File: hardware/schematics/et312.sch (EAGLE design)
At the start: 12 parts, among them IC1 MEGA16-P, IC2 4066N, X1 HD44780LCD-1602

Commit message: Updated Schematics
WIP
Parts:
- added JTAG: (no value), pinhead:PINHD-2X8
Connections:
- removed net N$9: 10WAY_RIBBON1.6
- new net 5V: 10WAY_RIBBON1.6, IC1.AREF, IC1.AVCC, IC1.VCC, IC2P.VDD, S1.P, S3.P
- new net JTAG11: JTAG.11
- new net JTAG13: JTAG.13
- new net JTAG15-RESET: IC1.RESET, JTAG.15
- new net JTAG7: JTAG.7
- new net JTAG9: JTAG.9
- new net N$6: IC1.(MISO)PB6
- new net PA1: 10WAY_RIBBON1.3, IC1.(ADC1)PA1
- new net PA4: 10WAY_RIBBON1.8, IC1.(ADC4)PA4
- new net PA5: 10WAY_RIBBON1.7, IC1.(ADC5)PA5
- net GND: now also 10WAY_RIBBON1.5, IC1.GND@1, IC2P.VSS

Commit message: PCB WIP
Added more to the PCB
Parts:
- added LED1, LED2: (no value), adafruit:LED3MM
- renumbered IC1 to U1, JTAG to J2
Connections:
- new net N$9: U1.(SS)PB4
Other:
- note added: "16 Way IDC connector"
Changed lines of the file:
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@@
 <?xml version="1.0" encoding="utf-8"?>
 <!DOCTYPE eagle SYSTEM "eagle.dtd">
-<eagle version="7.1.0">
+<eagle version="7.3.0">
 <drawing>
 <settings>
@@
 <part name="VR3" library="SparkFun-Electromechanical" deviceset="POT" device=""/>
 <part name="RV2" library="SparkFun-Electromechanical" deviceset="POT" device=""/>
-<part name="IC1" library="atmel" deviceset="MEGA16-P" device=""/>
+<part name="U1" library="atmel" deviceset="MEGA16-P" device=""/>
 <part name="S1" library="adafruit" deviceset="SPST" device=""/>
 <part name="S3" library="adafruit" deviceset="SPST" device=""/>
@@
 <part name="SUPPLY4" library="SparkFun-Aesthetics" deviceset="5V" device=""/>
 <part name="SUPPLY5" library="SparkFun-Aesthetics" deviceset="5V" device=""/>
-<part name="JTAG" library="pinhead" deviceset="PINHD-2X8" device=""/>
+<part name="J2" library="pinhead" deviceset="PINHD-2X8" device=""/>
+<part name="LED1" library="adafruit" deviceset="LED" device="3MM"/>
+<part name="LED2" library="adafruit" deviceset="LED" device="3MM"/>
+<part name="GND4" library="SparkFun-Aesthetics" deviceset="GND" device=""/>
 </parts>
 <sheets>
@@
 <sheet>
 <plain>
+<text x="35.56" y="119.38" size="1.778" layer="91">16 Way IDC connector</text>
 </plain>
 <instances>
 <instance part="FRAME1" gate="G$1" x="0" y="0"/>
 <instance part="GND1" gate="1" x="101.6" y="43.18"/>
-<instance part="IC1" gate="G$1" x="127" y="104.14"/>
+<instance part="U1" gate="G$1" x="127" y="104.14"/>
 <instance part="SUPPLY5" gate="G$1" x="99.06" y="149.86"/>
-<instance part="JTAG" gate="A" x="50.8" y="137.16"/>
+<instance part="J2" gate="A" x="50.8" y="137.16"/>
+<instance part="LED1" gate="G$1" x="205.74" y="71.12"/>
+<instance part="LED2" gate="G$1" x="215.9" y="71.12"/>
+<instance part="GND4" gate="1" x="210.82" y="43.18"/>
 </instances>
 <busses>
@@
 <net name="GND" class="0">
 <segment>
-<pinref part="IC1" gate="G$1" pin="GND"/>
+<pinref part="U1" gate="G$1" pin="GND"/>
 <wire x1="106.68" y1="114.3" x2="101.6" y2="114.3" width="0.1524" layer="91"/>
 <wire x1="101.6" y1="114.3" x2="101.6" y2="45.72" width="0.1524" layer="91"/>
 <pinref part="GND1" gate="1" pin="GND"/>
-<pinref part="IC1" gate="G$1" pin="GND@1"/>
+<pinref part="U1" gate="G$1" pin="GND@1"/>
 <wire x1="106.68" y1="121.92" x2="101.6" y2="121.92" width="0.1524" layer="91"/>
 <wire x1="101.6" y1="121.92" x2="101.6" y2="114.3" width="0.1524" layer="91"/>
@@
 <net name="PC0" class="0">
 <segment>
-<pinref part="IC1" gate="G$1" pin="(SCL)PC0"/>
+<pinref part="U1" gate="G$1" pin="(SCL)PC0"/>
 <wire x1="147.32" y1="81.28" x2="157.48" y2="81.28" width="0.1524" layer="91"/>
 <label x="157.48" y="81.28" size="1.778" layer="95" xref="yes"/>
@@
 <net name="PC4" class="0">
 <segment>
-<pinref part="IC1" gate="G$1" pin="(TDO)PC4"/>
+<pinref part="U1" gate="G$1" pin="(TDO)PC4"/>
 <wire x1="147.32" y1="91.44" x2="157.48" y2="91.44" width="0.1524" layer="91"/>
 <label x="157.48" y="91.44" size="1.778" layer="95" xref="yes"/>
@@
 <net name="PC5" class="0">
 <segment>
-<pinref part="IC1" gate="G$1" pin="(TDI)PC5"/>
+<pinref part="U1" gate="G$1" pin="(TDI)PC5"/>
 <wire x1="147.32" y1="93.98" x2="157.48" y2="93.98" width="0.1524" layer="91"/>
 <label x="157.48" y="93.98" size="1.778" layer="95" xref="yes"/>
@@
 <net name="PC6" class="0">
 <segment>
-<pinref part="IC1" gate="G$1" pin="(TOSC1)PC6"/>
+<pinref part="U1" gate="G$1" pin="(TOSC1)PC6"/>
 <wire x1="147.32" y1="96.52" x2="157.48" y2="96.52" width="0.1524" layer="91"/>
 <label x="157.48" y="96.52" size="1.778" layer="95" xref="yes"/>
@@
 <net name="PC7" class="0">
 <segment>
-<pinref part="IC1" gate="G$1" pin="(TOSC2)PC7"/>
+<pinref part="U1" gate="G$1" pin="(TOSC2)PC7"/>
 <wire x1="147.32" y1="99.06" x2="157.48" y2="99.06" width="0.1524" layer="91"/>
 <label x="157.48" y="99.06" size="1.778" layer="95" xref="yes"/>
@@
 <net name="PC3" class="0">
 <segment>
-<pinref part="IC1" gate="G$1" pin="(TMS)PC3"/>
+<pinref part="U1" gate="G$1" pin="(TMS)PC3"/>
 <wire x1="147.32" y1="88.9" x2="157.48" y2="88.9" width="0.1524" layer="91"/>
 <label x="157.48" y="88.9" size="1.778" layer="95" xref="yes"/>
@@
 <net name="PC2" class="0">
 <segment>
-<pinref part="IC1" gate="G$1" pin="(TCK)PC2"/>
+<pinref part="U1" gate="G$1" pin="(TCK)PC2"/>
 <wire x1="147.32" y1="86.36" x2="157.48" y2="86.36" width="0.1524" layer="91"/>
 <label x="157.48" y="86.36" size="1.778" layer="95" xref="yes"/>
@@
 <net name="PC1" class="0">
 <segment>
-<pinref part="IC1" gate="G$1" pin="(SDA)PC1"/>
+<pinref part="U1" gate="G$1" pin="(SDA)PC1"/>
 <wire x1="147.32" y1="83.82" x2="157.48" y2="83.82" width="0.1524" layer="91"/>
 <label x="157.48" y="83.82" size="1.778" layer="95" xref="yes"/>
@@
 <net name="PA5" class="0">
 <segment>
-<pinref part="IC1" gate="G$1" pin="(ADC5)PA5"/>
+<pinref part="U1" gate="G$1" pin="(ADC5)PA5"/>
 <wire x1="147.32" y1="139.7" x2="157.48" y2="139.7" width="0.1524" layer="91"/>
 <label x="157.48" y="139.7" size="1.778" layer="95" xref="yes"/>
@@
 <net name="PA4" class="0">
 <segment>
-<pinref part="IC1" gate="G$1" pin="(ADC4)PA4"/>
+<pinref part="U1" gate="G$1" pin="(ADC4)PA4"/>
 <wire x1="147.32" y1="137.16" x2="157.48" y2="137.16" width="0.1524" layer="91"/>
 <label x="157.48" y="137.16" size="1.778" layer="95" xref="yes"/>
@@
 <net name="PA1" class="0">
 <segment>
-<pinref part="IC1" gate="G$1" pin="(ADC1)PA1"/>
+<pinref part="U1" gate="G$1" pin="(ADC1)PA1"/>
 <wire x1="147.32" y1="129.54" x2="157.48" y2="129.54" width="0.1524" layer="91"/>
 <label x="157.48" y="129.54" size="1.778" layer="95" xref="yes"/>
@@
 <pinref part="SUPPLY5" gate="G$1" pin="5V"/>
 <wire x1="99.06" y1="149.86" x2="99.06" y2="127" width="0.1524" layer="91"/>
-<pinref part="IC1" gate="G$1" pin="AREF"/>
+<pinref part="U1" gate="G$1" pin="AREF"/>
 <wire x1="99.06" y1="127" x2="106.68" y2="127" width="0.1524" layer="91"/>
-<pinref part="IC1" gate="G$1" pin="AVCC"/>
+<pinref part="U1" gate="G$1" pin="AVCC"/>
 <wire x1="106.68" y1="124.46" x2="99.06" y2="124.46" width="0.1524" layer="91"/>
 <wire x1="99.06" y1="124.46" x2="99.06" y2="127" width="0.1524" layer="91"/>
-<pinref part="IC1" gate="G$1" pin="VCC"/>
+<pinref part="U1" gate="G$1" pin="VCC"/>
 <wire x1="106.68" y1="116.84" x2="99.06" y2="116.84" width="0.1524" layer="91"/>
 <wire x1="99.06" y1="116.84" x2="99.06" y2="124.46" width="0.1524" layer="91"/>
@@
 <net name="JTAG7" class="0">
 <segment>
-<pinref part="JTAG" gate="A" pin="7"/>
+<pinref part="J2" gate="A" pin="7"/>
 <wire x1="48.26" y1="137.16" x2="40.64" y2="137.16" width="0.1524" layer="91"/>
 <label x="40.64" y="137.16" size="1.778" layer="95" rot="R180" xref="yes"/>
@@
 <net name="JTAG9" class="0">
 <segment>
-<pinref part="JTAG" gate="A" pin="9"/>
+<pinref part="J2" gate="A" pin="9"/>
 <wire x1="48.26" y1="134.62" x2="40.64" y2="134.62" width="0.1524" layer="91"/>
 <label x="40.64" y="134.62" size="1.778" layer="95" rot="R180" xref="yes"/>
@@
 <net name="JTAG11" class="0">
 <segment>
-<pinref part="JTAG" gate="A" pin="11"/>
+<pinref part="J2" gate="A" pin="11"/>
 <wire x1="48.26" y1="132.08" x2="40.64" y2="132.08" width="0.1524" layer="91"/>
 <label x="40.64" y="132.08" size="1.778" layer="95" rot="R180" xref="yes"/>
@@
 <net name="JTAG13" class="0">
 <segment>
-<pinref part="JTAG" gate="A" pin="13"/>
+<pinref part="J2" gate="A" pin="13"/>
 <wire x1="48.26" y1="129.54" x2="40.64" y2="129.54" width="0.1524" layer="91"/>
 <label x="40.64" y="129.54" size="1.778" layer="95" rot="R180" xref="yes"/>
@@
 <net name="JTAG15-RESET" class="0">
 <segment>
-<pinref part="IC1" gate="G$1" pin="RESET"/>
+<pinref part="U1" gate="G$1" pin="RESET"/>
 <wire x1="106.68" y1="144.78" x2="96.52" y2="144.78" width="0.1524" layer="91"/>
 <label x="96.52" y="144.78" size="1.778" layer="95" rot="R180" xref="yes"/>
 </segment>
 <segment>
-<pinref part="JTAG" gate="A" pin="15"/>
+<pinref part="J2" gate="A" pin="15"/>
 <wire x1="48.26" y1="127" x2="40.64" y2="127" width="0.1524" layer="91"/>
 <label x="40.64" y="127" size="1.778" layer="95" rot="R180" xref="yes"/>
@@
 <net name="N$6" class="0">
 <segment>
-<pinref part="IC1" gate="G$1" pin="(MISO)PB6"/>
+<pinref part="U1" gate="G$1" pin="(MISO)PB6"/>
 <wire x1="147.32" y1="119.38" x2="157.48" y2="119.38" width="0.1524" layer="91"/>
-</segment>
-</net>
+<label x="157.48" y="119.38" size="1.778" layer="95" xref="yes"/>
+</segment>
+</net>
+<net name="N$9" class="0">
+<segment>
+<pinref part="U1" gate="G$1" pin="(SS)PB4"/>
+<wire x1="147.32" y1="114.3" x2="157.48" y2="114.3" width="0.1524" layer="91"/>
+<label x="157.48" y="114.3" size="1.778" layer="95" xref="yes"/>
+</segment>
+</net>

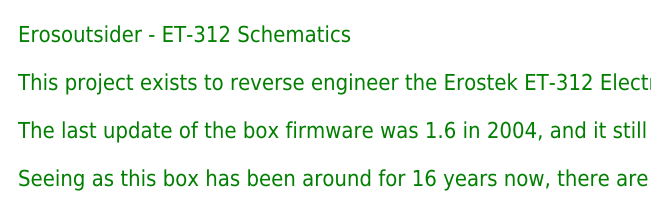
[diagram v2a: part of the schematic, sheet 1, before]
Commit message: update name on Pg1
Sheet one updated
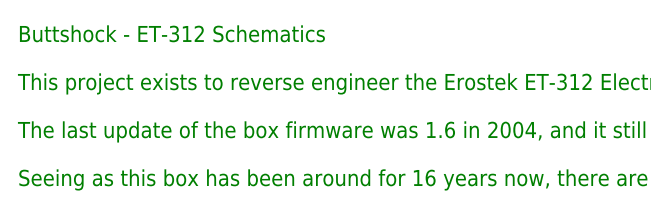
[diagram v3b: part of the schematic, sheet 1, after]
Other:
- note added: "Buttshock - ET-312 Schematics This project exists to reverse engineer the Erostek ET-312 Electrostimulation Device Firmware. The last update of the box firmware was 1.6 in 2004, and it still contains bugs and issues to this day. Seeing as this box has been around for 16 years now, there are probably hundreds of them around the world."
- note removed: "Erosoutsider - ET-312 Schematics This project exists to reverse engineer the Erostek ET-312 Electrostimulation Device Firmware. The last update of the box firmware was 1.6 in 2004, and it still contains bugs and issues to this day. Seeing as this box has been around for 16 years now, there are probably hundreds of them around the world."
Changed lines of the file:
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@@
 <sheet>
 <plain>
-<text x="12.7" y="152.4" size="1.778" layer="91">Erosoutsider - ET-312 Schematics
+<text x="12.7" y="152.4" size="1.778" layer="91">Buttshock - ET-312 Schematics
 This project exists to reverse engineer the Erostek ET-312 Electrostimulation Device Firmware.
 The last update of the box firmware was 1.6 in 2004, and it still contains bugs and issues to this day.

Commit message: updated with output stage
brought in Flocked's output stage, WIP
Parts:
- added C1, C4: (no value), SparkFun-Passives:CAP_POLPTH1
- added C2, C3: (no value), SparkFun-Passives:CAPPTH
- added IC3: LM358, SparkFun-AnalogIC:LM358
- added IC4, IC6: 7809, adafruit:7805T
- added IC5: LTC1661, linear-technology:LTC2602CMS8
- added IC7: 7805, adafruit:7805T
- added Q1, Q2, Q4, Q5: IRL520N-H, transistor-fet-1:IRL530N-H
- added Q3, Q6: IRF9Z24, transistor-fet-1:IRL530N-H
- added R1, R11, R12, R16, R17, R18, R19, R21, R22, R4, R6, R7, R8, R9: 100k, eagle-ltspice:R0207/10
- added R10, R20: 200k, eagle-ltspice:R0207/10
- added R13, R14, R15, R2, R3, R5: 10k, eagle-ltspice:R0207/10
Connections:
- new net N$18: Q1.G, R2.2
- new net N$19: Q2.G, R3.2
- new net N$20: IC3G1.OUT, R5.1, R6.2
- new net N$21: C2.1, Q3.G, R5.2
- new net N$22: IC3G1.+IN, R11.2, R7.2, R8.1
- new net N$24: Q4.G, R13.2
- new net N$25: Q5.G, R14.2
- new net N$26: IC3G2.OUT, R15.1, R16.2
- new net N$27: C3.1, Q6.G, R15.2
- new net N$28: IC3G2.-IN, R17.2, R18.1, R22.2
- new net N$33: IC5.VOUTB, R22.1
- new net N$34: Q1.D
- new net N$35: Q3.D
- new net N$36: Q4.D
- new net N$37: Q6.D
- new net N$38: Q5.D
- new net N$39: Q2.D
- new net N$40: IC3G1.-IN, R10.2, R6.1, R9.1
- new net N$41: IC3G2.+IN, R16.1, R19.1, R20.2
- new net N$42: IC5.VOUTA, R11.1
- new net PA0: Q1.S, Q2.S, Q4.S, Q5.S
- new net PB0: R14.1, R21.2
- new net PB1: R12.2, R13.1
- new net PB2: R3.1, R4.2
- new net PB3: R1.2, R2.1
- new net PB5: IC5.SDI
- new net PB7: IC5.SCK
- new net PD4: IC5.!CS/LD
- new net VCC: C1.+, C2.2, C3.2, C4.+, IC3G1.V+, IC4.VO, IC5.REF, IC5.VCC, IC6.VO, IC7.VO, Q3.S, Q6.S, R18.2, R19.2, R8.2, R9.2
- net GND: now also C1.-, C4.-, IC3G1.V-, IC4.GND, IC5.GND, IC6.GND, IC7.GND, R1.1, R10.1, R12.1, R17.1, R20.1, R21.1, R4.1, R7.1
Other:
- note added: "Output Stage"

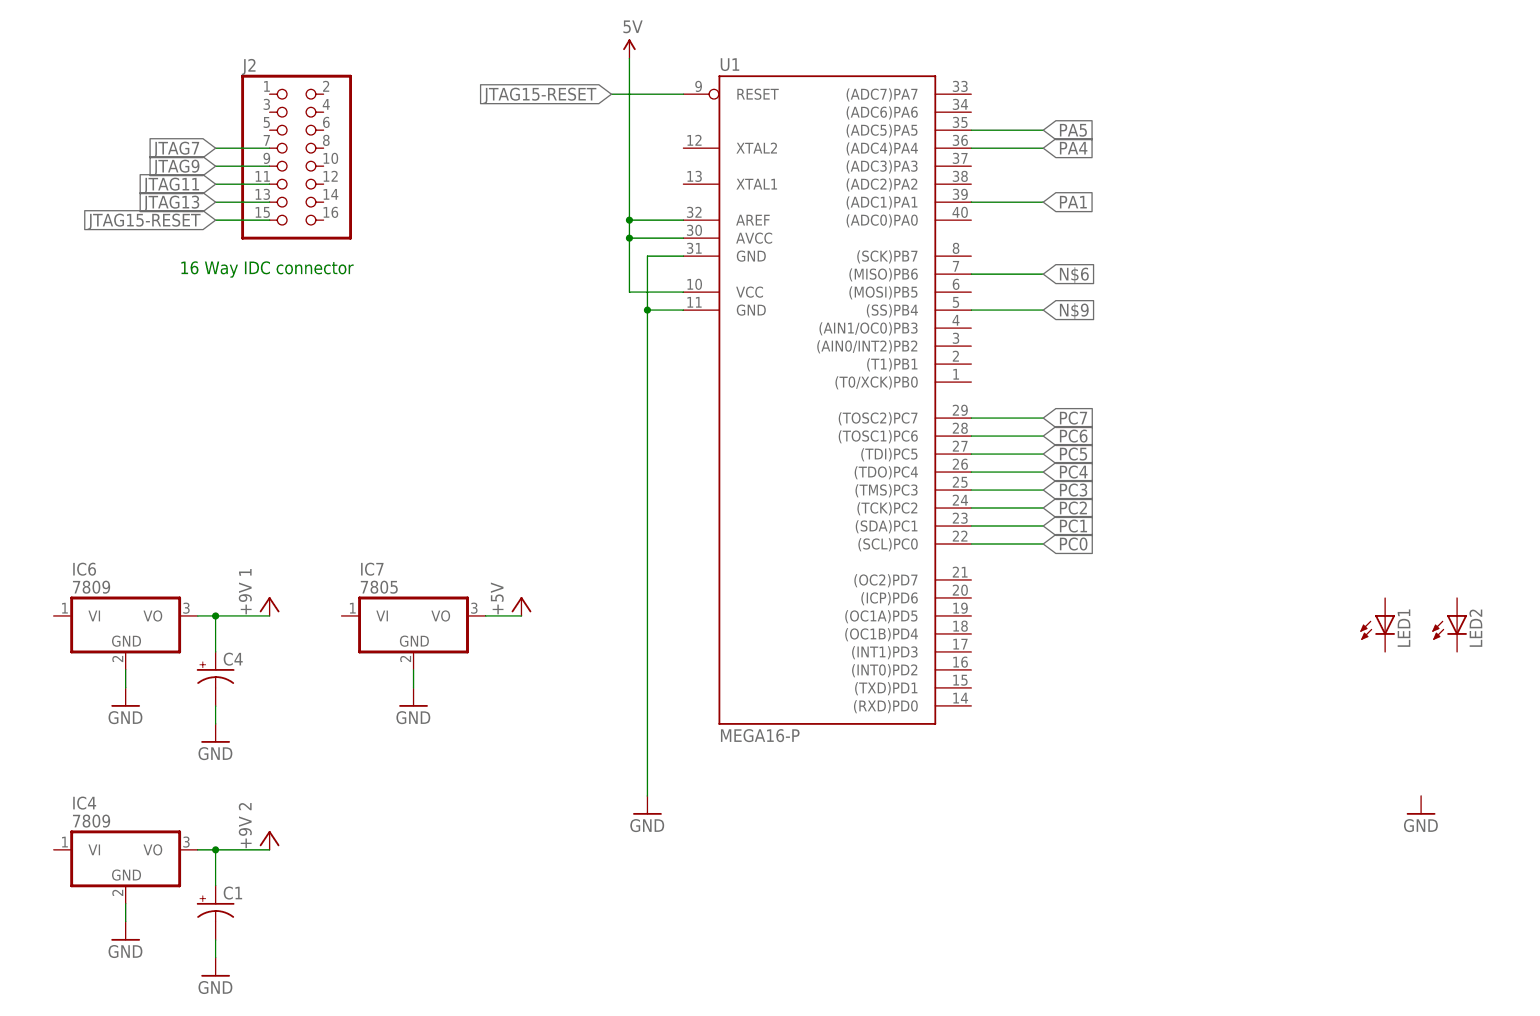
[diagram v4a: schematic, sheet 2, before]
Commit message: Schematics
Name Nets
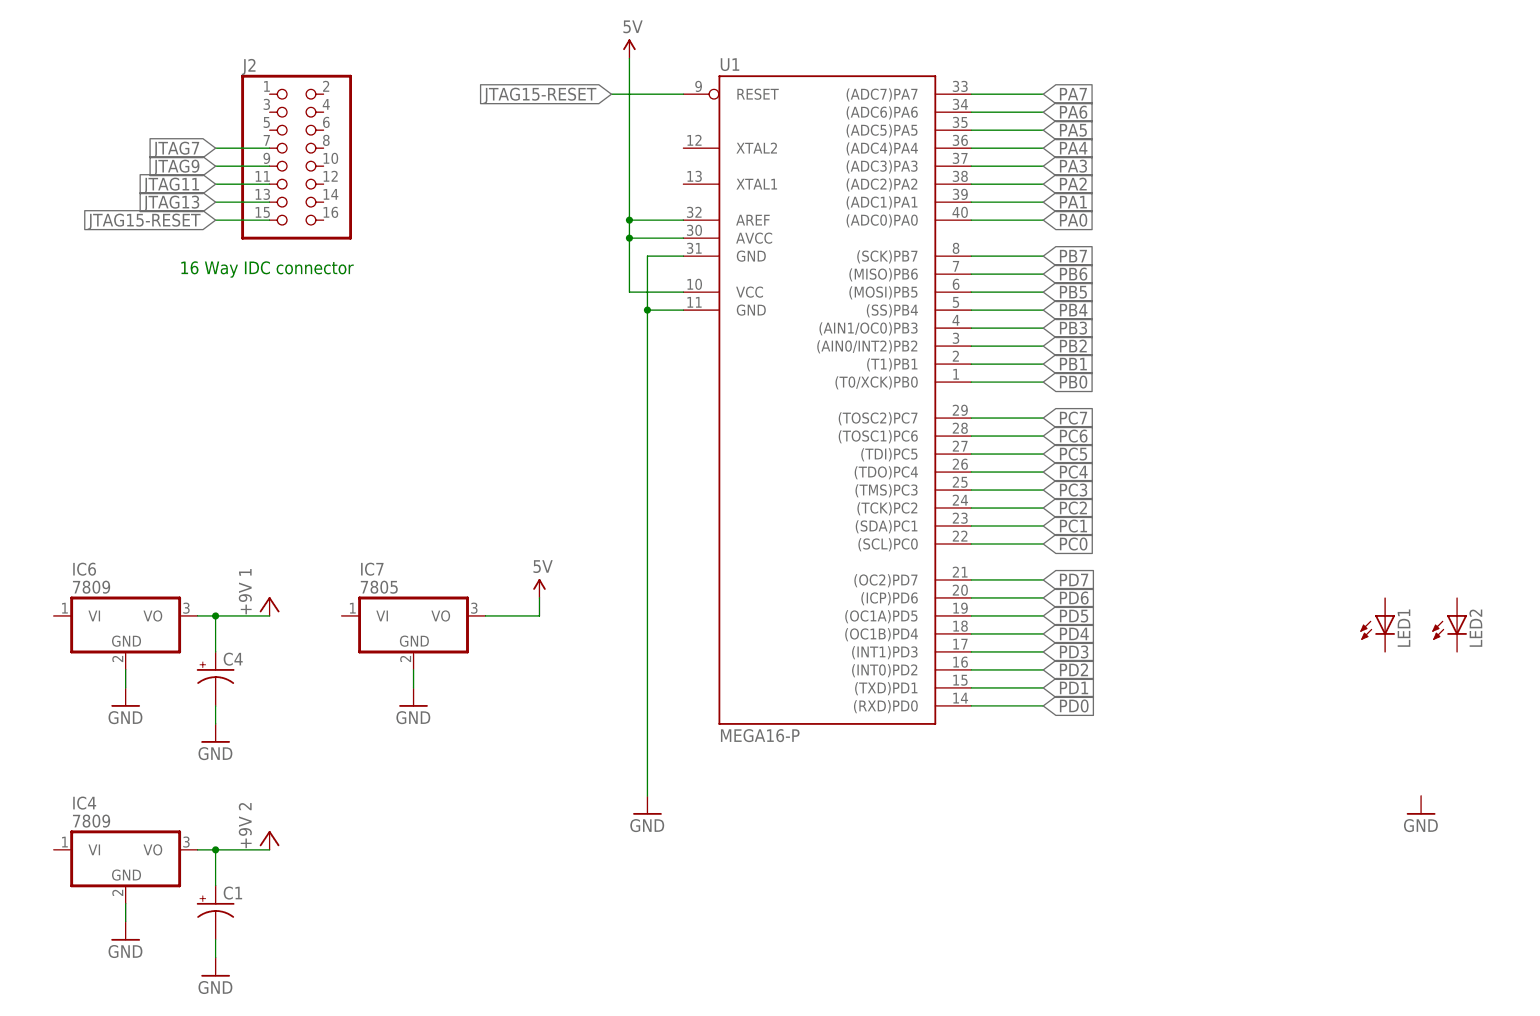
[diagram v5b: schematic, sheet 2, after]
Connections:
- net N$6 renamed PB6
- net N$9 renamed PB4
- new net PA2: U1.(ADC2)PA2
- new net PA3: U1.(ADC3)PA3
- new net PA6: U1.(ADC6)PA6
- new net PA7: U1.(ADC7)PA7
- new net PD0: U1.(RXD)PD0
- new net PD1: U1.(TXD)PD1
- new net PD2: U1.(INT0)PD2
- new net PD3: U1.(INT1)PD3
- new net PD5: U1.(OC1A)PD5
- new net PD6: U1.(ICP)PD6
- new net PD7: U1.(OC2)PD7
- net 5V: now also IC7.VO
- net PA0: now also U1.(ADC0)PA0
- net PB0: now also U1.(T0/XCK)PB0
- net PB1: now also U1.(T1)PB1
- net PB2: now also U1.(AIN0/INT2)PB2
- net PB3: now also U1.(AIN1/OC0)PB3
- net PB5: now also U1.(MOSI)PB5
- net PB7: now also U1.(SCK)PB7
- net PD4: now also U1.(OC1B)PD4
- net VCC: no longer IC7.VO
